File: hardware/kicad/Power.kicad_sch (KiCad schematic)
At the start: 6 parts

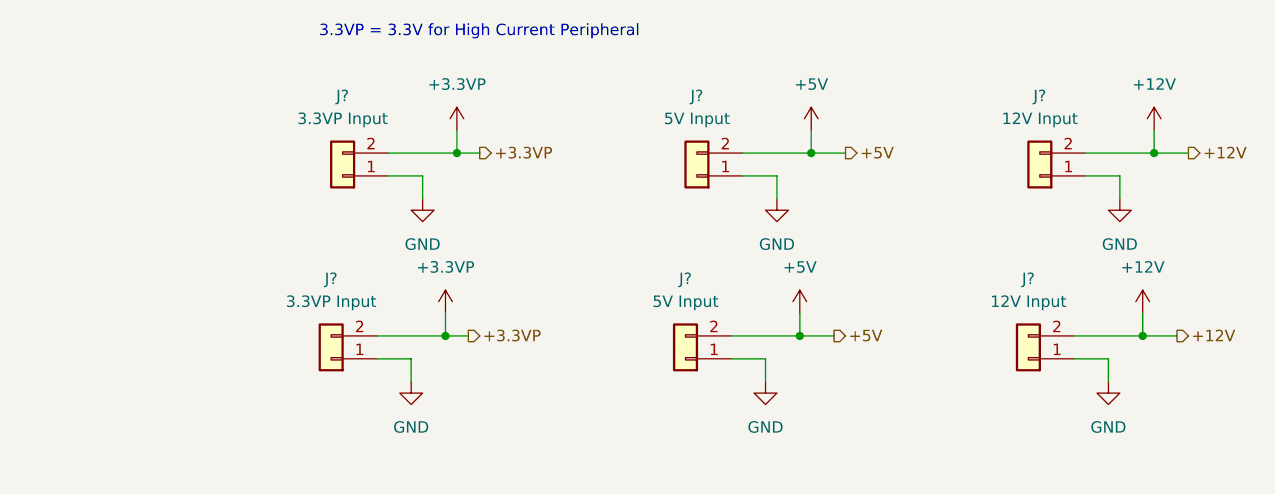
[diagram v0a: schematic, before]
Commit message: update schematic
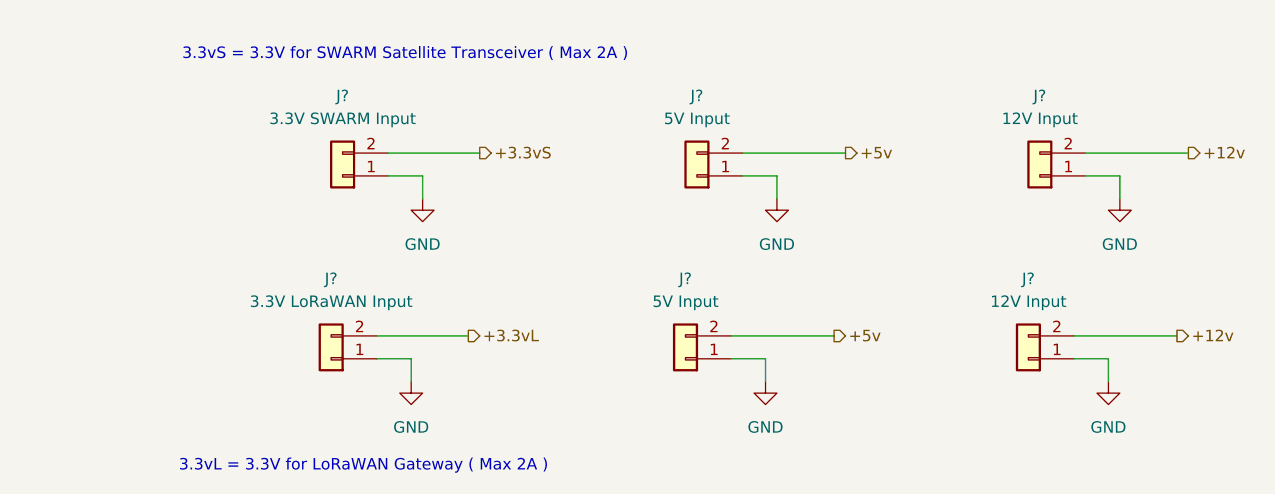
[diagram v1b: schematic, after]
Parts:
- J?: value 3.3VP Input -> 3.3V SWARM Input
- J?: value 3.3VP Input -> 3.3V LoRaWAN Input
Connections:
- net +12V renamed +12v
- net +3.3VP renamed +3.3vL
- net +3.3vL: no longer J?.2 (Pin_2)
- net +5V renamed +5v
- new net +3.3vS: J?.2 (Pin_2)
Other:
- note added: "3.3vL = 3.3V for LoRaWAN Gateway ( Max 2A )"
- note added: "3.3vS = 3.3V for SWARM Satellite Transceiver ( Max 2A )"
- note removed: "3.3VP = 3.3V for High Current Peripheral"
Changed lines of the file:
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@@
 (kicad_sch (version 20211123) (generator eeschema)
   (paper "A4")
-  (junction (at 166.37 80.01) (diameter 0) (color 0 0 0 0)
-  )
-  (junction (at 167.64 59.69) (diameter 0) (color 0 0 0 0)
-  )
-  (junction (at 128.27 80.01) (diameter 0) (color 0 0 0 0)
-  )
-  (junction (at 129.54 59.69) (diameter 0) (color 0 0 0 0)
-  )
-  (junction (at 88.9 80.01) (diameter 0) (color 0 0 0 0)
-  )
-  (junction (at 90.17 59.69) (diameter 0) (color 0 0 0 0)
-  )
-  (wire (pts (xy 166.37 77.47) (xy 166.37 80.01))
+  (wire (pts (xy 81.28 80.01) (xy 91.44 80.01))
     (stroke (width 0) (type default) (color 0 0 0 0))
   )
-  (wire (pts (xy 128.27 80.01) (xy 132.08 80.01))
+  (wire (pts (xy 82.55 59.69) (xy 92.71 59.69))
     (stroke (width 0) (type default) (color 0 0 0 0))
   )
-  (wire (pts (xy 88.9 80.01) (xy 91.44 80.01))
-    (stroke (width 0) (type default) (color 0 0 0 0))
-  )
-  (wire (pts (xy 90.17 59.69) (xy 92.71 59.69))
-    (stroke (width 0) (type default) (color 0 0 0 0))
-  )
-  (wire (pts (xy 128.27 80.01) (xy 120.65 80.01))
+  (wire (pts (xy 120.65 80.01) (xy 132.08 80.01))
     (stroke (width 0) (type default) (color 0 0 0 0))
   )
@@
     (stroke (width 0) (type default) (color 0 0 0 0))
   )
-  (wire (pts (xy 90.17 57.15) (xy 90.17 59.69))
-    (stroke (width 0) (type default) (color 0 0 0 0))
-  )
-  (wire (pts (xy 88.9 77.47) (xy 88.9 80.01))
-    (stroke (width 0) (type default) (color 0 0 0 0))
-  )
-  (wire (pts (xy 88.9 80.01) (xy 81.28 80.01))
-    (stroke (width 0) (type default) (color 0 0 0 0))
-  )
-  (wire (pts (xy 129.54 59.69) (xy 133.35 59.69))
+  (wire (pts (xy 121.92 59.69) (xy 133.35 59.69))
     (stroke (width 0) (type default) (color 0 0 0 0))
   )
@@
     (stroke (width 0) (type default) (color 0 0 0 0))
   )
-  (wire (pts (xy 129.54 59.69) (xy 121.92 59.69))
-    (stroke (width 0) (type default) (color 0 0 0 0))
-  )
-  (wire (pts (xy 167.64 59.69) (xy 160.02 59.69))
-    (stroke (width 0) (type default) (color 0 0 0 0))
-  )
-  (wire (pts (xy 166.37 80.01) (xy 170.18 80.01))
+  (wire (pts (xy 160.02 59.69) (xy 171.45 59.69))
     (stroke (width 0) (type default) (color 0 0 0 0))
   )
@@
   )
   (wire (pts (xy 162.56 82.55) (xy 162.56 85.09))
-    (stroke (width 0) (type default) (color 0 0 0 0))
-  )
-  (wire (pts (xy 90.17 59.69) (xy 82.55 59.69))
-    (stroke (width 0) (type default) (color 0 0 0 0))
-  )
-  (wire (pts (xy 167.64 57.15) (xy 167.64 59.69))
-    (stroke (width 0) (type default) (color 0 0 0 0))
-  )
-  (wire (pts (xy 128.27 77.47) (xy 128.27 80.01))
     (stroke (width 0) (type default) (color 0 0 0 0))
   )
@@
     (stroke (width 0) (type default) (color 0 0 0 0))
   )
-  (wire (pts (xy 166.37 80.01) (xy 158.75 80.01))
+  (wire (pts (xy 158.75 80.01) (xy 170.18 80.01))
     (stroke (width 0) (type default) (color 0 0 0 0))
   )
@@
   )
   (wire (pts (xy 85.09 82.55) (xy 85.09 85.09))
-    (stroke (width 0) (type default) (color 0 0 0 0))
-  )
-  (wire (pts (xy 129.54 57.15) (xy 129.54 59.69))
     (stroke (width 0) (type default) (color 0 0 0 0))
   )
@@
     (stroke (width 0) (type default) (color 0 0 0 0))
   )
-  (wire (pts (xy 167.64 59.69) (xy 171.45 59.69))
-    (stroke (width 0) (type default) (color 0 0 0 0))
-  )
-  (text "3.3VP = 3.3V for High Current Peripheral" (at 110.49 46.99 180)
+  (text "3.3vS = 3.3V for SWARM Satellite Transceiver ( Max 2A )"
+    (at 109.22 49.53 0)
     (effects (font (size 1.27 1.27)) (justify right bottom))
   )
-  (hierarchical_label "+12V" (shape output) (at 170.18 80.01 0)
+  (text "3.3vL = 3.3V for LoRaWAN Gateway ( Max 2A )" (at 100.33 95.25 180)
+    (effects (font (size 1.27 1.27)) (justify right bottom))
+  )
+  (hierarchical_label "+12v" (shape output) (at 170.18 80.01 0)
     (effects (font (size 1.27 1.27)) (justify left))
   )
-  (hierarchical_label "+3.3VP" (shape output) (at 92.71 59.69 0)
+  (hierarchical_label "+3.3vS" (shape output) (at 92.71 59.69 0)
     (effects (font (size 1.27 1.27)) (justify left))
   )
-  (hierarchical_label "+5V" (shape output) (at 133.35 59.69 0)
+  (hierarchical_label "+5v" (shape output) (at 133.35 59.69 0)
     (effects (font (size 1.27 1.27)) (justify left))
   )
-  (hierarchical_label "+3.3VP" (shape output) (at 91.44 80.01 0)
+  (hierarchical_label "+3.3vL" (shape output) (at 91.44 80.01 0)
     (effects (font (size 1.27 1.27)) (justify left))
   )
-  (hierarchical_label "+12V" (shape output) (at 171.45 59.69 0)
+  (hierarchical_label "+12v" (shape output) (at 171.45 59.69 0)
     (effects (font (size 1.27 1.27)) (justify left))
   )
-  (hierarchical_label "+5V" (shape output) (at 132.08 80.01 0)
+  (hierarchical_label "+5v" (shape output) (at 132.08 80.01 0)
     (effects (font (size 1.27 1.27)) (justify left))
   )
@@
     (pin "2")
   )
-  (symbol (lib_id "power:+12V") (at 167.64 57.15 0) (unit 1)
-    (in_bom yes) (on_board yes) (fields_autoplaced)
-    (property "Reference" "#PWR?" (id 0) (at 167.64 60.96 0)
-      (effects (font (size 1.27 1.27)) hide)
-    )
-    (property "Value" "+12V" (id 1) (at 167.64 52.07 0))
-    (property "Footprint" "" (id 2) (at 167.64 57.15 0)
-      (effects (font (size 1.27 1.27)) hide)
-    )
-    (property "Datasheet" "" (id 3) (at 167.64 57.15 0)
-      (effects (font (size 1.27 1.27)) hide)
-    )
-    (pin "1")
-  )
   (symbol (lib_id "power:GND") (at 124.46 85.09 0) (unit 1)
     (in_bom yes) (on_board yes) (fields_autoplaced)
@@
     )
     (property "Datasheet" "" (id 3) (at 124.46 85.09 0)
-      (effects (font (size 1.27 1.27)) hide)
-    )
-    (pin "1")
-  )
-  (symbol (lib_id "power:+3.3VP") (at 90.17 57.15 0) (unit 1)
-    (in_bom yes) (on_board yes) (fields_autoplaced)
-    (property "Reference" "#PWR?" (id 0) (at 93.98 58.42 0)
-      (effects (font (size 1.27 1.27)) hide)
-    )
-    (property "Value" "+3.3VP" (id 1) (at 90.17 52.07 0))
-    (property "Footprint" "" (id 2) (at 90.17 57.15 0)
-      (effects (font (size 1.27 1.27)) hide)
-    )
-    (property "Datasheet" "" (id 3) (at 90.17 57.15 0)
       (effects (font (size 1.27 1.27)) hide)
     )
@@
     (pin "1")
   )
-  (symbol (lib_id "power:+12V") (at 166.37 77.47 0) (unit 1)
-    (in_bom yes) (on_board yes) (fields_autoplaced)
-    (property "Reference" "#PWR?" (id 0) (at 166.37 81.28 0)
-      (effects (font (size 1.27 1.27)) hide)
-    )
-    (property "Value" "+12V" (id 1) (at 166.37 72.39 0))
-    (property "Footprint" "" (id 2) (at 166.37 77.47 0)
-      (effects (font (size 1.27 1.27)) hide)
-    )
-    (property "Datasheet" "" (id 3) (at 166.37 77.47 0)
-      (effects (font (size 1.27 1.27)) hide)
-    )
-    (pin "1")
-  )
   (symbol (lib_id "Connector_Generic:Conn_01x02") (at 77.47 62.23 180) (unit 1)
     (in_bom yes) (on_board yes) (fields_autoplaced)
     (property "Reference" "J?" (id 0) (at 77.47 53.34 0))
-    (property "Value" "3.3VP Input" (id 1) (at 77.47 55.88 0))
+    (property "Value" "3.3V SWARM Input" (id 1) (at 77.47 55.88 0))
     (property "Footprint" "" (id 2) (at 77.47 62.23 0)
       (effects (font (size 1.27 1.27)) hide)
@@
     (pin "2")
   )
-  (symbol (lib_id "power:+5V") (at 129.54 57.15 0) (unit 1)
-    (in_bom yes) (on_board yes) (fields_autoplaced)
-    (property "Reference" "#PWR?" (id 0) (at 129.54 60.96 0)
-      (effects (font (size 1.27 1.27)) hide)
-    )
-    (property "Value" "+5V" (id 1) (at 129.54 52.07 0))
-    (property "Footprint" "" (id 2) (at 129.54 57.15 0)
-      (effects (font (size 1.27 1.27)) hide)
-    )
-    (property "Datasheet" "" (id 3) (at 129.54 57.15 0)
-      (effects (font (size 1.27 1.27)) hide)
-    )
-    (pin "1")
-  )
   (symbol (lib_id "Connector_Generic:Conn_01x02") (at 76.2 82.55 180) (unit 1)
     (in_bom yes) (on_board yes) (fields_autoplaced)
     (property "Reference" "J?" (id 0) (at 76.2 73.66 0))
-    (property "Value" "3.3VP Input" (id 1) (at 76.2 76.2 0))
+    (property "Value" "3.3V LoRaWAN Input" (id 1) (at 76.2 76.2 0))
     (property "Footprint" "" (id 2) (at 76.2 82.55 0)
       (effects (font (size 1.27 1.27)) hide)
@@
     (pin "1")
     (pin "2")
-  )
-  (symbol (lib_id "power:+3.3VP") (at 88.9 77.47 0) (unit 1)
-    (in_bom yes) (on_board yes) (fields_autoplaced)
-    (property "Reference" "#PWR?" (id 0) (at 92.71 78.74 0)
-      (effects (font (size 1.27 1.27)) hide)
-    )
-    (property "Value" "+3.3VP" (id 1) (at 88.9 72.39 0))
-    (property "Footprint" "" (id 2) (at 88.9 77.47 0)
-      (effects (font (size 1.27 1.27)) hide)
-    )
-    (property "Datasheet" "" (id 3) (at 88.9 77.47 0)
-      (effects (font (size 1.27 1.27)) hide)
-    )
-    (pin "1")
   )
   (symbol (lib_id "power:GND") (at 85.09 85.09 0) (unit 1)
@@
       (effects (font (size 1.27 1.27)) hide)
     )
-    (pin "1")
-  )
-  (symbol (lib_id "power:+5V") (at 128.27 77.47 0) (unit 1)
-    (in_bom yes) (on_board yes) (fields_autoplaced)
-    (property "Reference" "#PWR?" (id 0) (at 128.27 81.28 0)
-      (effects (font (size 1.27 1.27)) hide)
-    )
-    (property "Value" "+5V" (id 1) (at 128.27 72.39 0))
-    (property "Footprint" "" (id 2) (at 128.27 77.47 0)
-      (effects (font (size 1.27 1.27)) hide)
-    )
-    (property "Datasheet" "" (id 3) (at 128.27 77.47 0)
-      (effects (font (size 1.27 1.27)) hide)
-    )

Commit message: initial pcb design
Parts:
- removed J?: 5V Input, symbol Connector_Generic:Conn_01x02
- removed J?: 12V Input, symbol Connector_Generic:Conn_01x02
- added C31, C32, C33, C34, C36, C37, C38, C39, C40, C41, C42, C43: 10u, Capacitor_SMD:C_0805_2012Metric, symbol Device:C
- added C35, C44, C45: 100uF, Capacitor_Tantalum_SMD:CP_EIA-7343-31_Kemet-D, symbol Device:CP
- added TP21: 3.3v LoRaWAN, TestPoint:TestPoint_Pad_D1.0mm, symbol Connector:TestPoint
- added TP22: 3.3v SWARM, TestPoint:TestPoint_Pad_D1.0mm, symbol Connector:TestPoint
- added TP23: 5v, TestPoint:TestPoint_Pad_D1.0mm, symbol Connector:TestPoint
- added TP24: 12v, TestPoint:TestPoint_Pad_D1.0mm, symbol Connector:TestPoint
- added TP25, TP26: GND, TestPoint:TestPoint_Pad_D1.0mm, symbol Connector:TestPoint
- J1: renamed from J?; value 3.3V LoRaWAN Input -> 3.3V LoRaWAN; footprint (none) -> Connector_Wire:SolderWire-0.5sqmm_1x02_P4.8mm_D0.9mm_OD2.3mm
- J2: renamed from J?; value 3.3V SWARM Input -> 3.3V SWARM; footprint (none) -> Connector_Wire:SolderWire-0.5sqmm_1x02_P4.8mm_D0.9mm_OD2.3mm
- J4: renamed from J?; value 5V Input -> 5V; footprint (none) -> Connector_Wire:SolderWire-0.5sqmm_1x02_P4.8mm_D0.9mm_OD2.3mm
- J6: renamed from J?; value 12V Input -> 12V; footprint (none) -> Connector_Wire:SolderWire-0.5sqmm_1x02_P4.8mm_D0.9mm_OD2.3mm
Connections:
- net +12v: now also TP24.1
- net +3.3vL: now also C36.1, C38.1, C40.1, C42.1, C44.1, TP21.1
- net +3.3vS: now also C31.1, C32.1, C33.1, C34.1, C35.1, TP22.1
- net +5v: now also C37.1, C39.1, C41.1, C43.1, C45.1, TP23.1
- net GND: now also C31.2, C32.2, C33.2, C34.2, C35.2, C36.2, C37.2, C38.2, C39.2, C40.2, C41.2, C42.2, C43.2, C44.2, C45.2, TP25.1, TP26.1
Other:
- note added: "5V for Raspberry Pi CM4 ( Max 2A )"
- note added: "Power Input"
- note added: "Power Input Debuggging"
- moved on the sheet: J1, J2, J4, J6
